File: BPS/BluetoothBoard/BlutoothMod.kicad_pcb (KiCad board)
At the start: 2 copper layers, 13 parts, among them J1 Conn_01x06, SW1 SW_DIP_x01, U1 RN4870-V_RM118, U2 MCP100-315D

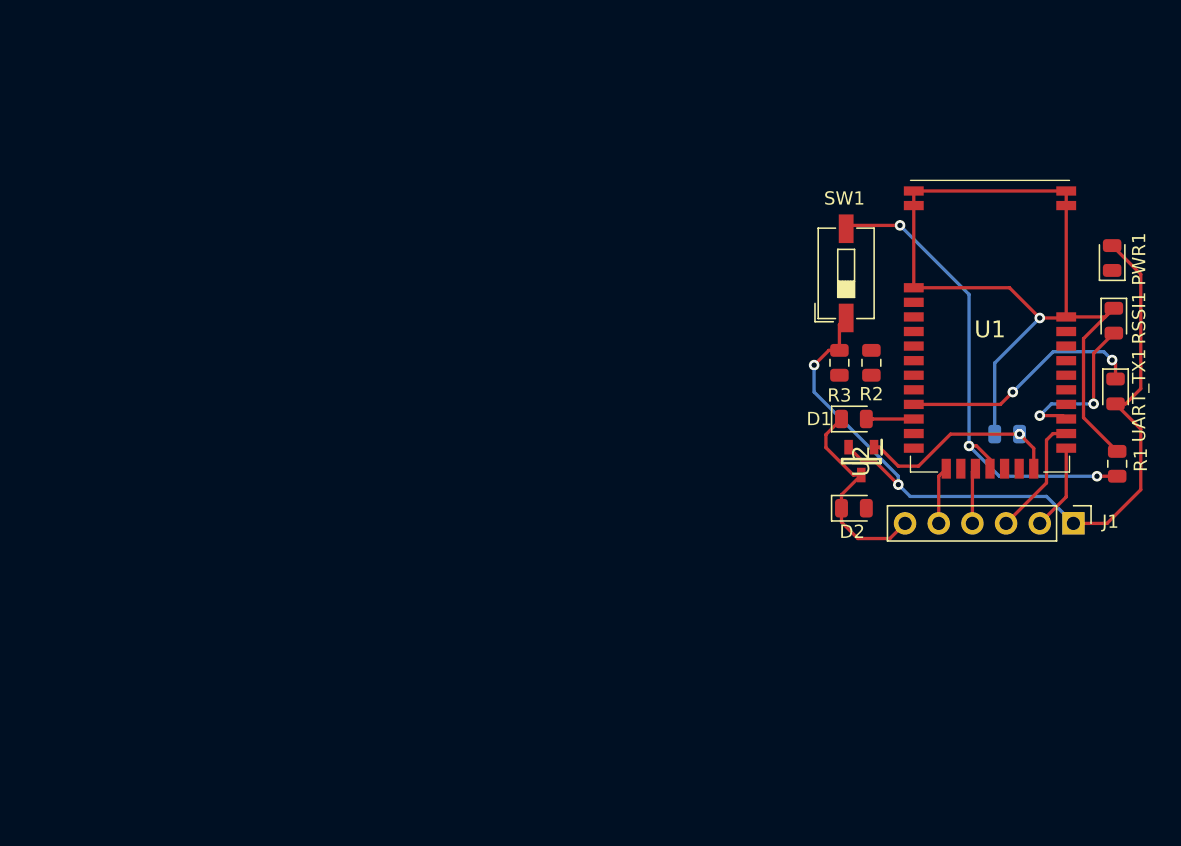
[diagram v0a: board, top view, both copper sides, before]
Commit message: Finished master board. Working to make sure that bluetooth mount won't cover anything important on master board, yet still be big enough to hold everything.
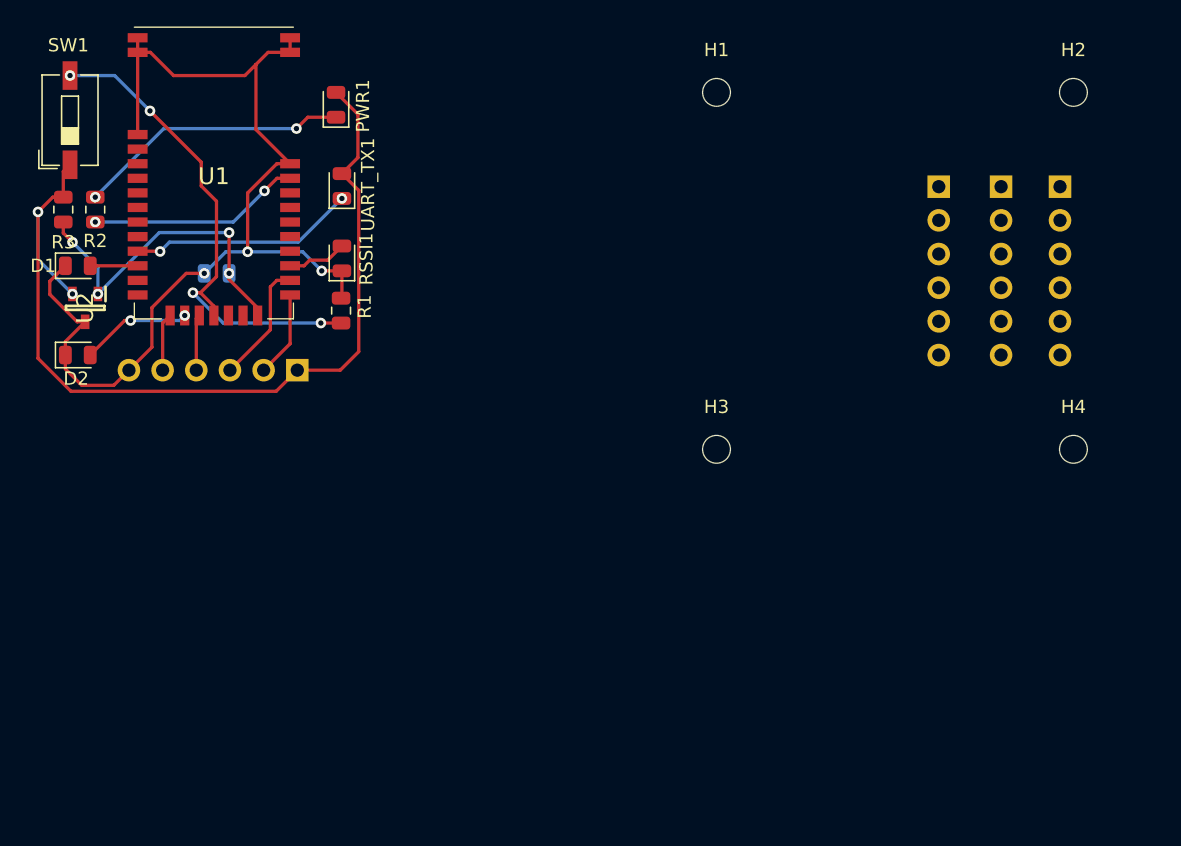
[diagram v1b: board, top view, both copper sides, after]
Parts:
- added H1: MountingHole, MountingHole:MountingHole_2.1mm, F.Cu at (116.7, 85.2)
- added H2: MountingHole, MountingHole:MountingHole_2.1mm, F.Cu at (143.6, 85.2)
- added H3: MountingHole, MountingHole:MountingHole_2.1mm, F.Cu at (116.7, 112.1)
- added H4: MountingHole, MountingHole:MountingHole_2.1mm, F.Cu at (143.6, 112.1)
- added J2: Conn_01x06, Connector_PinSocket_2.54mm:PinSocket_1x06_P2.54mm_Vertical, B.Cu at (142.6, 92.3)
- added J3: Conn_01x06, Connector_PinSocket_2.54mm:PinSocket_1x06_P2.54mm_Vertical, B.Cu at (138.2, 92.3)
- added J4: Conn_01x06, Connector_PinSocket_2.54mm:PinSocket_1x06_P2.54mm_Vertical, B.Cu at (133.5, 92.3)
- J1: footprint Connector_PinHeader_2.54mm:PinHeader_1x06_P2.54mm_Vertical -> Connector_PinSocket_2.54mm:PinSocket_1x06_P2.54mm_Vertical; moved to B.Cu
- moved C1 60.8 mm to (79.0, 98.9)
- moved UART_TX1 60.4 mm to (88.5, 92.3), turned to 90 degrees
- moved D1 59.7 mm to (68.5, 98.3)
- moved D2 59.7 mm to (68.5, 105.0)
- moved SW1 59.7 mm to (67.9, 87.3)
- moved U2 59.7 mm to (69.1, 101.5)
- moved J1 59.7 mm to (85.1, 106.2), turned to 90 degrees
- moved PWR1 59.7 mm to (88.0, 86.2)
- moved R1 59.7 mm to (88.4, 101.7)
- moved R2 59.7 mm to (69.8, 94.1)
- moved R3 59.7 mm to (67.4, 94.1)
- moved U1 59.7 mm to (78.8, 91.3)
- moved RSSI1 58.4 mm to (88.5, 97.7), turned to 90 degrees
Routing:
- net Net-(PWR1-Pad1): track 0.00 -> 20.7 mm, vias 0 -> 2
- net Net-(R2-Pad1): track 0.00 -> 16.1 mm, vias 0 -> 2
- net Net-(C1-Pad1): track 15.6 -> 25.5 mm, vias 1 -> 4
- net Net-(D2-Pad2): track 0.00 -> 8.36 mm, vias 0 -> 2
- net Net-(RSSI1-Pad2): track 12.5 -> 4.53 mm, vias 2 -> 0
- net +3V3: track 63.5 -> 71.1 mm
- net GND: track 83.7 -> 78.8 mm, vias 1 -> 3
- net Net-(U1-Pad11): track 18.4 -> 17.1 mm
- net Net-(R1-Pad1): track 37.8 -> 38.3 mm, vias 3 -> 4

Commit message: Finished Bluetooth board. Entire board wouldn't fit inside mount so the board is extended past the mounting holes. Still need to replace footprint of interface pins with connectors that go through the board.
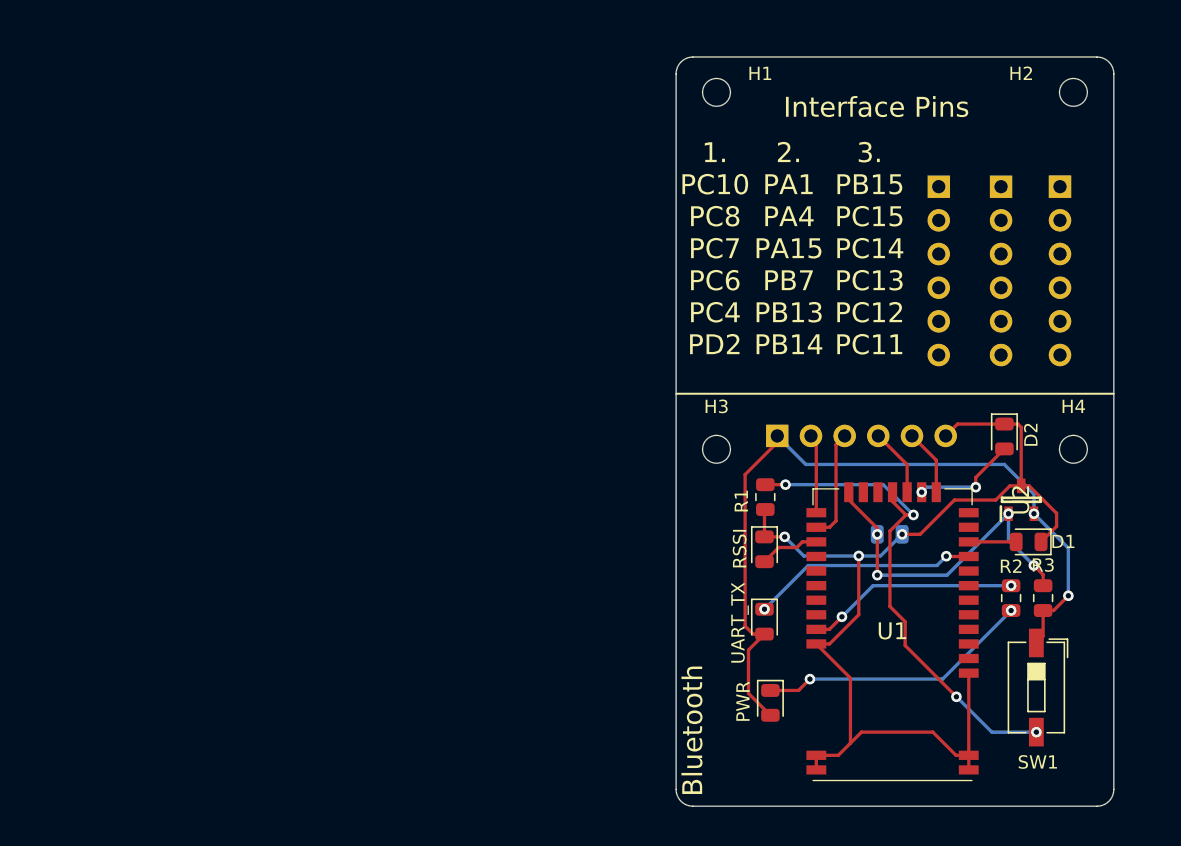
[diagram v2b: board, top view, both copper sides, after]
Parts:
- added G***: LOGO, UTSVT_Special:UTSVT_Logo_Symbol, B.Cu at (122.6, 101.0)
- added G***: LOGO, UTSVT_Special:Hallock_Image_Tiny, B.Cu at (127.6, 90.2)
- moved SW1 84.5 mm to (140.8, 130.1), turned to 270 degrees
- moved R3 79.5 mm to (141.4, 123.4), turned to 90 degrees
- moved R2 75.0 mm to (138.9, 123.4), turned to 270 degrees
- moved D1 74.7 mm to (140.3, 119.1), turned to 180 degrees
- moved U2 72.1 mm to (139.7, 116.0), turned to 90 degrees
- moved D2 70.2 mm to (138.4, 111.2), turned to 270 degrees
- moved U1 61.9 mm to (130.0, 126.1), turned to 180 degrees
- moved PWR 55.8 mm to (120.8, 131.3), turned to 270 degrees
- moved C1 54.5 mm to (129.8, 118.6), turned to 0 degrees
- moved UART_TX 45.8 mm to (120.3, 125.1), turned to 270 degrees
- moved RSSI 38.7 mm to (120.3, 119.7), turned to 270 degrees
- moved J1 36.5 mm to (121.3, 111.1), turned to 270 degrees
- moved R1 35.0 mm to (120.4, 115.7), turned to 270 degrees
- renumbered PWR1 to PWR, RSSI1 to RSSI, UART_TX1 to UART_TX
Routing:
- net +3V3: track 71.1 -> 59.3 mm
- net /UART_RTS: track 4.22 -> 5.47 mm
- net /UART_TX: track 9.24 -> 8.37 mm
- net GND: track 78.8 -> 79.4 mm
- net /UART_CTS: track 4.36 -> 5.00 mm
- net /UART_RX: track 6.50 -> 5.96 mm
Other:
- board outline added: 33 x 56.5 mm
- board text added: "1. PC10 PC8 PC7 PC6 PC4 PD2"
- board text added: "2. PA1 PA4 PA15 PB7 PB13 PB14"
- board text added: "3. PB15 PC15 PC14 PC13 PC12 PC11"
- board text added: "Bluetooth"
- board text added: "Interface Pins"

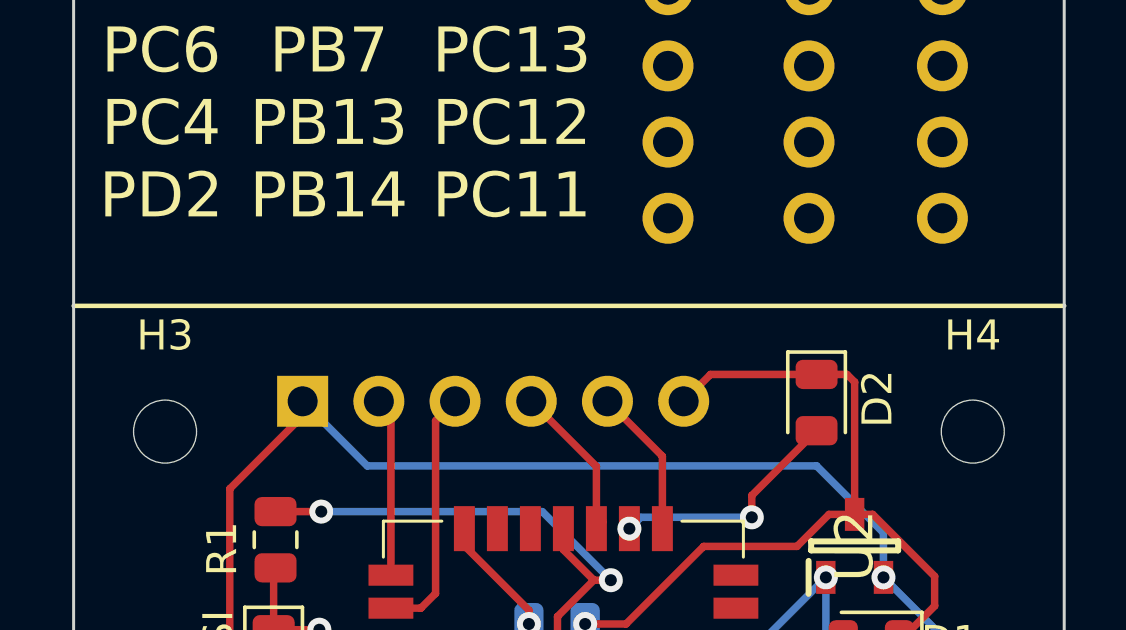
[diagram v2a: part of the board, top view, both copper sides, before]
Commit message: Added references to board
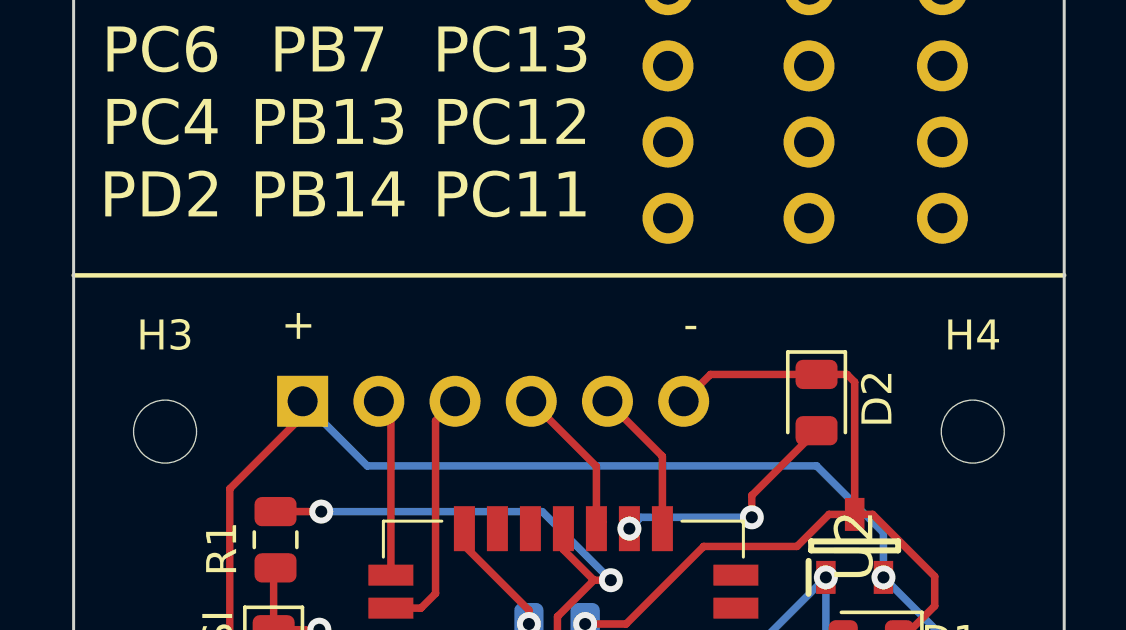
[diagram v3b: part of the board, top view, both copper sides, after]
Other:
- board text added: "+"
- board text added: "-"

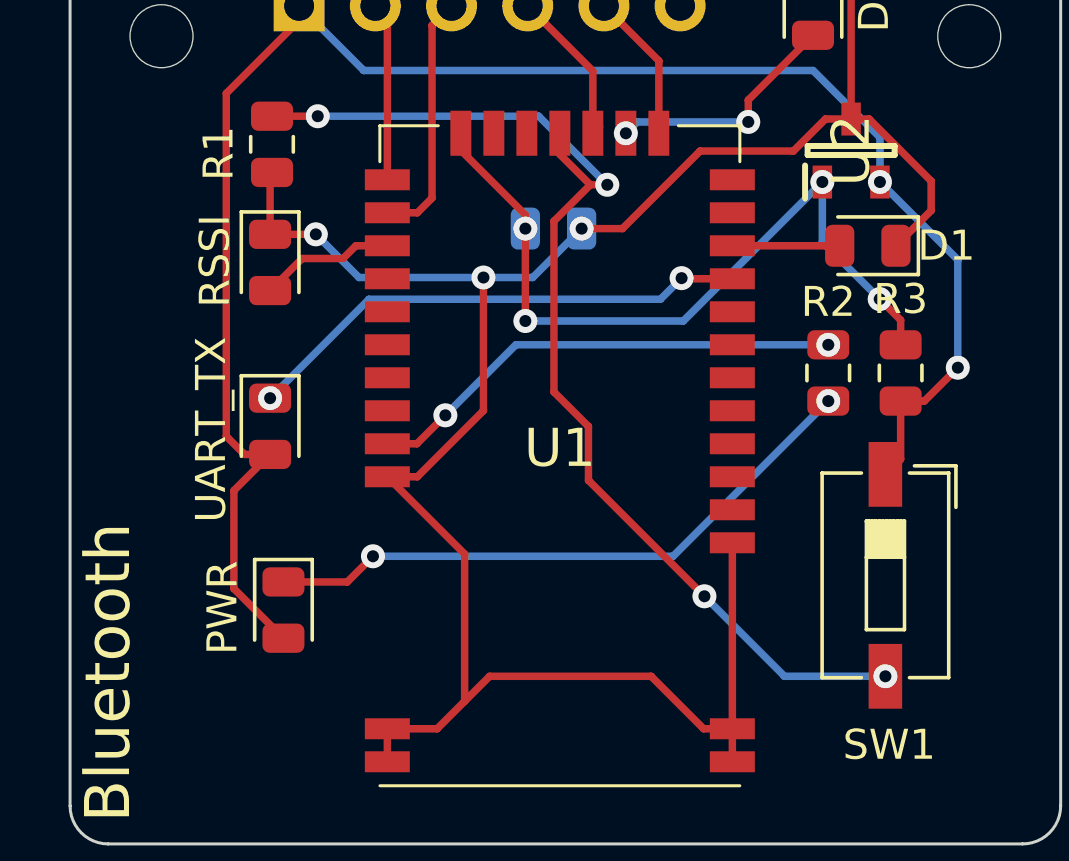
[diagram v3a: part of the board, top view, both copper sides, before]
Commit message: Connected power to Bluetooth Module
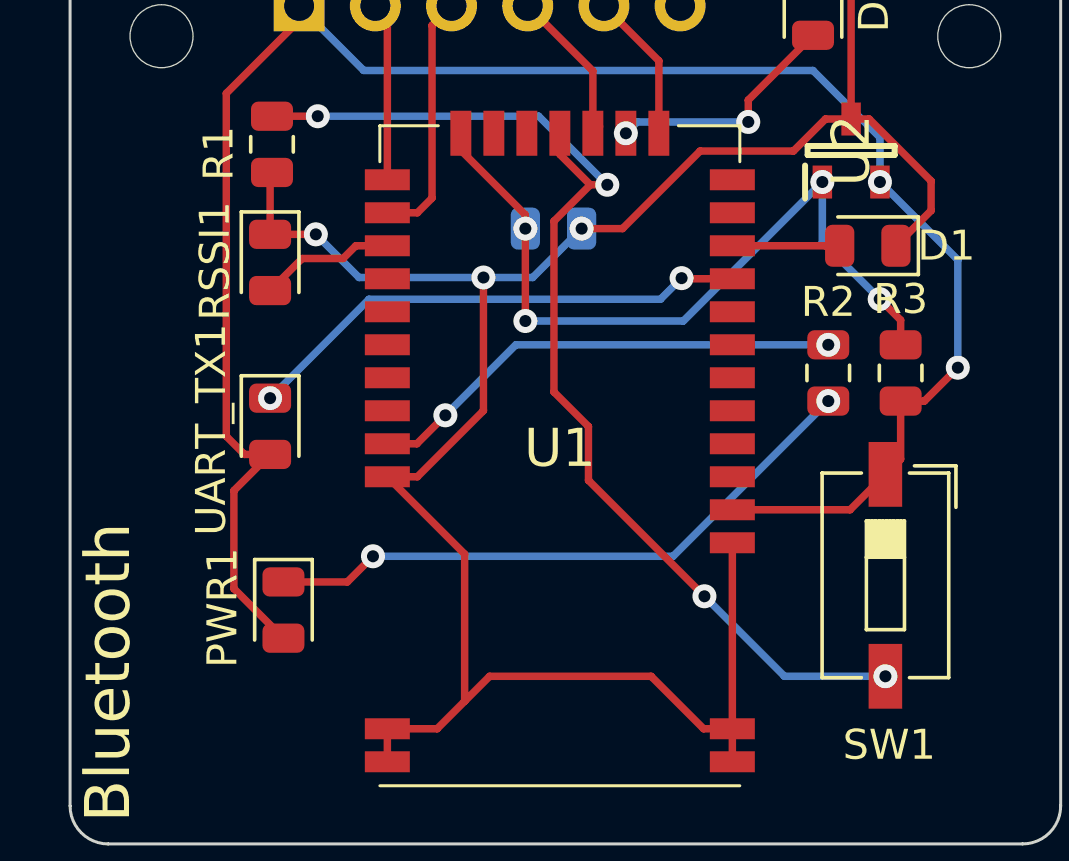
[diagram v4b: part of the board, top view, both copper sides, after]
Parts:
- removed G***: LOGO, UTSVT_Special:UTSVT_Logo_Symbol
- removed G***: LOGO, UTSVT_Special:Hallock_Image_Tiny
- renumbered PWR to PWR1, RSSI to RSSI1, UART_TX to UART_TX1
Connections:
- U1 pad 4: Net-(U1-Pad4) -> +3V3
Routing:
- net +3V3: track 59.3 -> 64.9 mm
